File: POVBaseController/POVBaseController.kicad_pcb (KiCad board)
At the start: 2 copper layers, 24 parts, among them P1 CONN_01X02, P2 CONN_01X02, P3 CONN_01X05, U1 MPM3606, U2 CY8C4014LQI-412

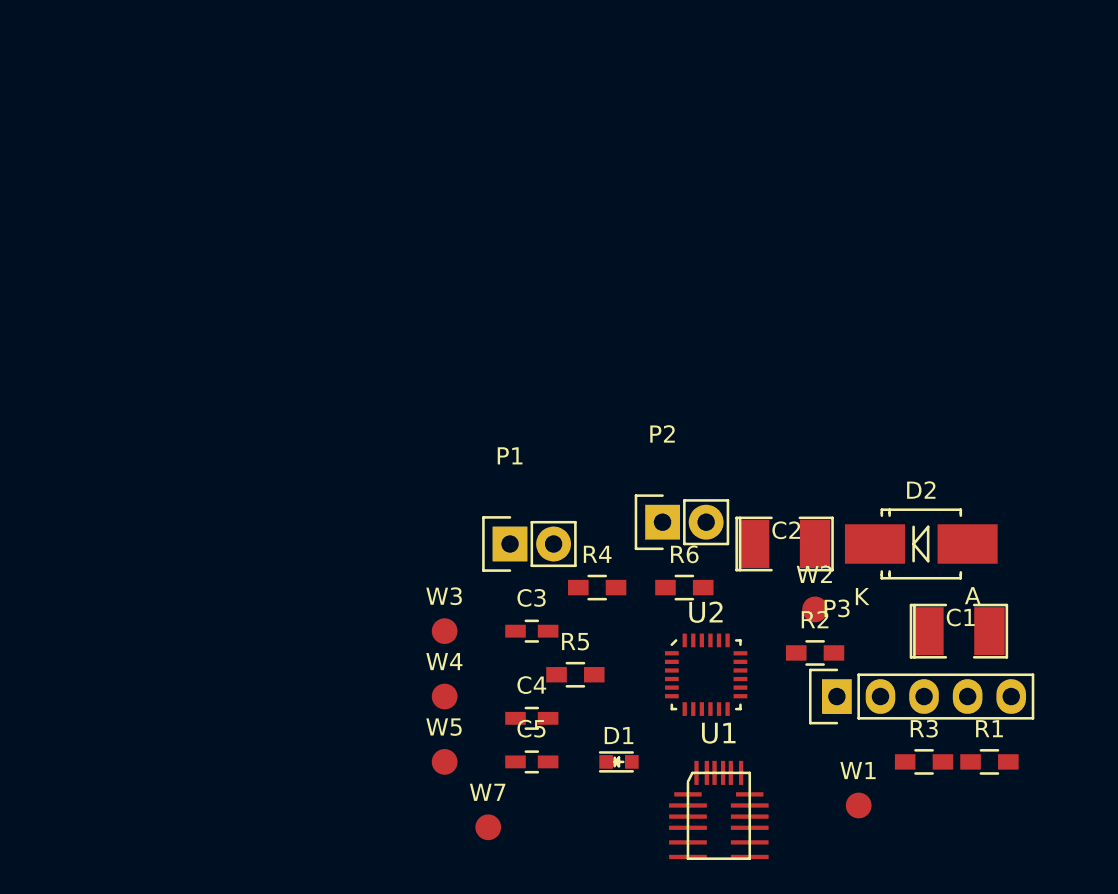
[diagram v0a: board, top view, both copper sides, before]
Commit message: Updated the design and layout with an LDO.
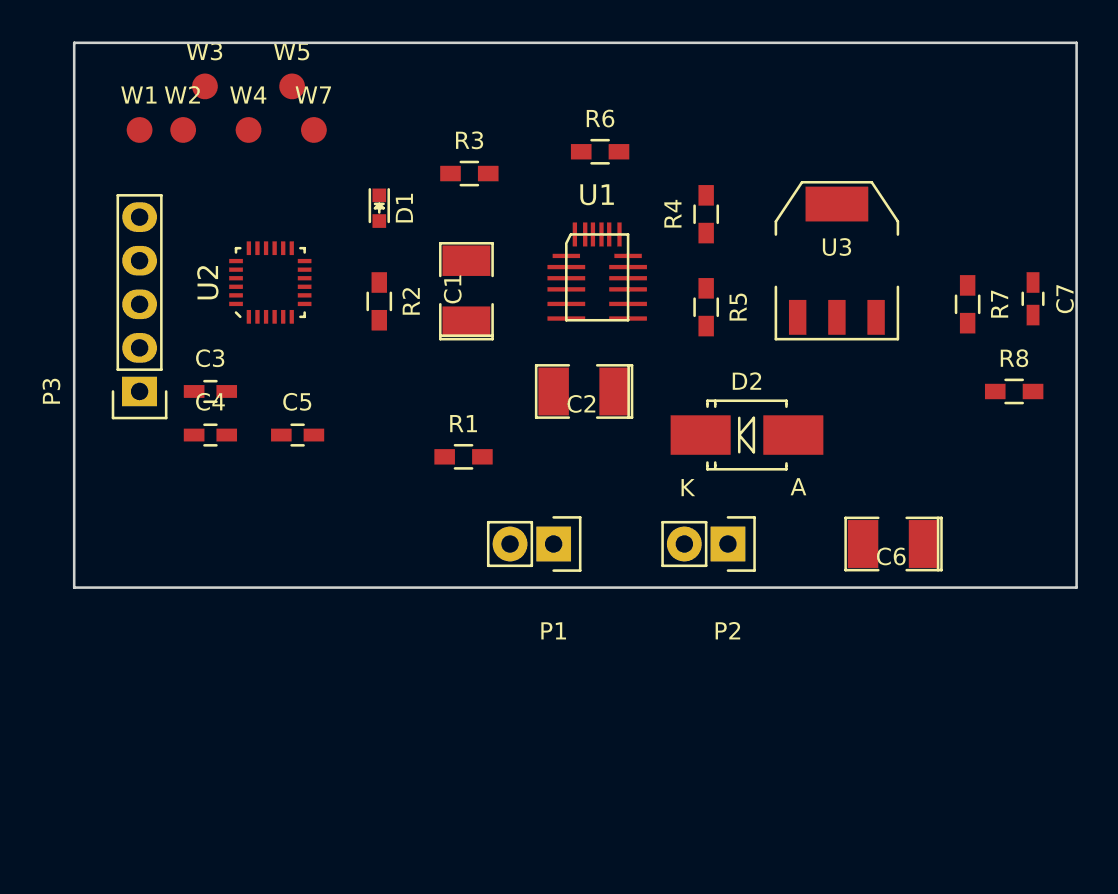
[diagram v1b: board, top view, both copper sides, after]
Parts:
- added C6: 10u, SMD_Packages:SMD-1210_Pol, F.Cu at (159.5, 97.8)
- added C7: 100u, Capacitors_SMD:C_0603_HandSoldering, F.Cu at (167.6, 83.5)
- added R7: 120, Resistors_SMD:R_0603_HandSoldering, F.Cu at (163.8, 83.8)
- added R8: 360, Resistors_SMD:R_0603_HandSoldering, F.Cu at (166.5, 88.9)
- added U3: LD1117S50CTR, TO_SOT_Packages_SMD:SOT-223, F.Cu at (156.2, 81.3)
- moved W1 57.5 mm to (115.6, 73.7)
- moved W2 46.2 mm to (118.1, 73.7)
- moved P3 44.4 mm to (115.6, 88.9), turned to 90 degrees
- moved R3 43.3 mm to (134.8, 76.2)
- moved W7 41.9 mm to (125.7, 73.7)
- moved W5 40.4 mm to (124.5, 71.1)
- moved R1 35.4 mm to (134.4, 92.7)
- moved D1 35.2 mm to (129.5, 78.2), turned to 270 degrees
- moved W4 34.9 mm to (121.9, 73.7)
- moved C1 34.9 mm to (134.6, 83.1), turned to 90 degrees
- moved W3 34.7 mm to (119.4, 71.1)
- moved U2 34.2 mm to (123.2, 82.5), turned to 90 degrees
- moved R2 32.6 mm to (129.5, 83.7), turned to 270 degrees
- moved U1 32.2 mm to (142.2, 82.5)
- moved R6 25.9 mm to (142.4, 74.9)
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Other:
- board outline added: 58.4 x 31.8 mm

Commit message: Completed the routing of the POVBaseController.
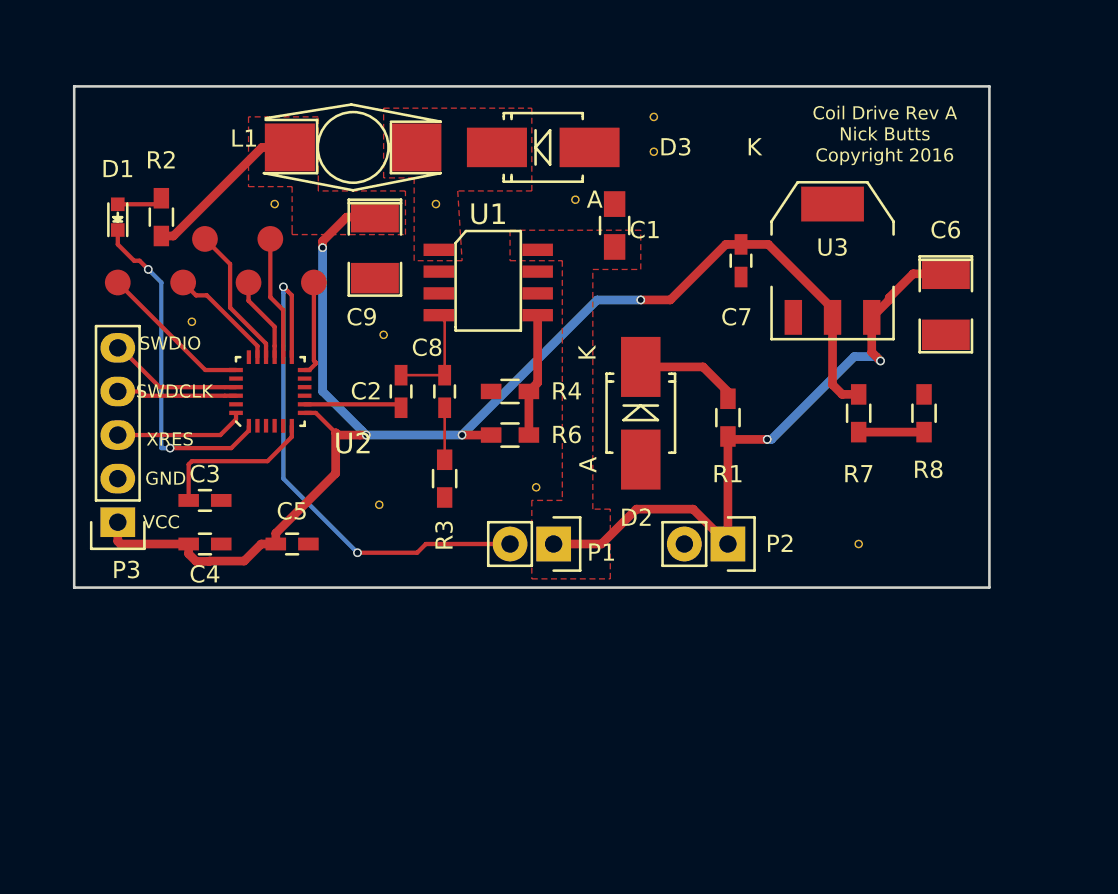
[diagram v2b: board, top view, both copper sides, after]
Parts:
- removed R5: 100K, Resistors_SMD:R_0603_HandSoldering
- added C8: 8.2n, Capacitors_SMD:C_0603_HandSoldering, F.Cu at (133.3, 88.9)
- added C9: 22u, SMD_Packages:SMD-1210_Pol, F.Cu at (129.3, 80.5)
- added D3: STPS2L40, Diodes_SMD:SMB_Handsoldering, F.Cu at (139.1, 74.7)
- added L1: 82u, myfootprint:TDK_Inductor_12.95x9.4x5.08, F.Cu at (128.0, 74.7)
- added REF**: VIA-13MILS, myfootprint:VIA-13MILS, F.Cu at (118.6, 84.8)
- added REF**: VIA-13MILS, myfootprint:VIA-13MILS, F.Cu at (157.5, 97.8)
- added REF**: VIA-13MILS, myfootprint:VIA-13MILS, F.Cu at (145.5, 72.9)
- added REF**: VIA-13MILS, myfootprint:VIA-13MILS, F.Cu at (145.5, 74.9)
- added REF**: VIA-13MILS, myfootprint:VIA-13MILS, F.Cu at (141.0, 77.7)
- added REF**: VIA-13MILS, myfootprint:VIA-13MILS, F.Cu at (132.8, 78.0)
- added REF**: VIA-13MILS, myfootprint:VIA-13MILS, F.Cu at (123.4, 78.0)
- added REF**: VIA-13MILS, myfootprint:VIA-13MILS, F.Cu at (129.8, 85.6)
- added REF**: VIA-13MILS, myfootprint:VIA-13MILS, F.Cu at (129.5, 95.5)
- added REF**: VIA-13MILS, myfootprint:VIA-13MILS, F.Cu at (138.7, 94.5)
- C1: value 10U -> 1.5u; footprint SMD_Packages:SMD-1210_Pol -> Capacitors_SMD:C_0805_HandSoldering
- C2: value 22U -> 56p; footprint SMD_Packages:SMD-1210_Pol -> Capacitors_SMD:C_0603_HandSoldering
- R3: value 100K -> 11k
- R4: value 100K -> 4.3k
- R6: value 19.1K -> 13k
- U1: value MPM3606 -> A5970AD; footprint myfootprint:QFN-20 -> myfootprint:SO-8
- moved R3 17.8 mm to (133.3, 94.0), turned to 270 degrees
- moved R6 17.3 mm to (137.2, 91.4), turned to 180 degrees
- moved C7 17.2 mm to (150.6, 81.3)
- moved R1 15.6 mm to (149.9, 90.4), turned to 90 degrees
- moved R4 15.4 mm to (137.2, 88.9), turned to 180 degrees
- moved D1 15.2 mm to (114.3, 78.7), turned to 90 degrees
- moved C6 14.3 mm to (162.6, 83.8), turned to 270 degrees
- moved R2 13.6 mm to (116.8, 78.7)
- moved C2 10.7 mm to (130.8, 88.9), turned to 270 degrees
- moved C1 9.45 mm to (143.3, 79.2)
- moved R7 8.98 mm to (157.5, 90.2)
- moved W1 8.98 mm to (114.3, 82.5)
- moved W5 8.98 mm to (123.2, 80.0)
- moved W2 8.89 mm to (118.1, 82.5)
- moved W3 8.89 mm to (119.4, 80.0)
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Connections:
- C2 pad 1: VCC -> Net-(C2-Pad1)
- R3 pad 1: +12V -> Net-(C8-Pad2)
- R3 pad 2: Net-(R3-Pad2) -> GND
- R4 pad 1: VCC -> Net-(R4-Pad1)
- R4 pad 2: Net-(R4-Pad2) -> GND
- R6 pad 1: Net-(R5-Pad2) -> Net-(R4-Pad1)
- R6 pad 2: GND -> VCC
- U1 pad 1: Net-(R5-Pad2) -> Net-(D3-Pad1)
- U1 pad 2: Net-(U1-Pad2) -> (no net)
- U1 pad 4: Net-(U1-Pad4) -> Net-(C2-Pad1)
- U1 pad 5: Net-(U1-Pad5) -> Net-(R4-Pad1)
- U1 pad 6: Net-(U1-Pad6) -> (no net)
- U1 pad 7: VCC -> GND
- U1 pad 8: VCC -> +12V
- U2 pad 10: Net-(U2-Pad10) -> (no net)
- U2 pad 11: Net-(U2-Pad11) -> (no net)
- U2 pad 2: Net-(U2-Pad2) -> (no net)
- U2 pad 20: Net-(U2-Pad20) -> (no net)
- U2 pad 23: Net-(U2-Pad23) -> (no net)
- U2 pad 3: Net-(U2-Pad3) -> (no net)
- U2 pad 4: Net-(U2-Pad4) -> (no net)
- U2 pad 5: Net-(U2-Pad5) -> (no net)
- U2 pad 9: Net-(U2-Pad9) -> (no net)
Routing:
- net VCC: track 0.00 -> 90.8 mm, vias 0 -> 4
- net +12V: track 0.00 -> 37.6 mm, vias 0 -> 2
- net /COIL_DR: track 0.00 -> 30.7 mm, vias 0 -> 2
- net /LED: track 0.00 -> 19.8 mm, vias 0 -> 2
- net GND: track 0.00 -> 9.55 mm
- net Net-(C3-Pad1): track 0.00 -> 9.42 mm
- net Net-(U2-Pad19): track 0.00 -> 9.00 mm
- net Net-(U2-Pad16): track 0.00 -> 8.36 mm
- net /SWDIO: track 0.00 -> 7.84 mm
- net /XRES: track 0.00 -> 7.64 mm
- net Net-(U2-Pad14): track 0.00 -> 7.20 mm
- net Net-(R4-Pad1): track 0.00 -> 7.20 mm
- net /SWDCLK: track 0.00 -> 6.99 mm
- net Net-(U2-Pad17): track 0.00 -> 6.51 mm
- net Net-(C2-Pad1): track 0.00 -> 6.18 mm
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- added copper zone on F.Cu, net +12V
- added copper zone on B.Cu, net GND
- added copper zone on F.Cu, net GND
- added copper zone on F.Cu, net Net-(D3-Pad1)
- added copper zone on F.Cu, net VCC
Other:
- board size 58.4 x 31.8 mm -> 53.3 x 29.2 mm
- rule trace_min: 0.2 -> 0.1524
- rule via_min_size: 0.4 -> 0.3302
- board text added: "Coil Drive Rev A Nick Butts Copyright 2016"
- board text added: "GND"
- board text added: "SWDCLK"
- board text added: "SWDIO"
- board text added: "VCC"
- board text added: "XRES"

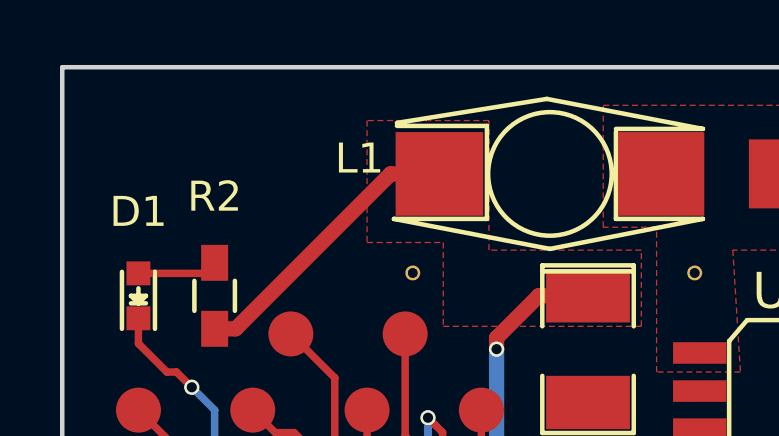
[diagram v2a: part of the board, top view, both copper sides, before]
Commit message: Ordering the POVBaseController
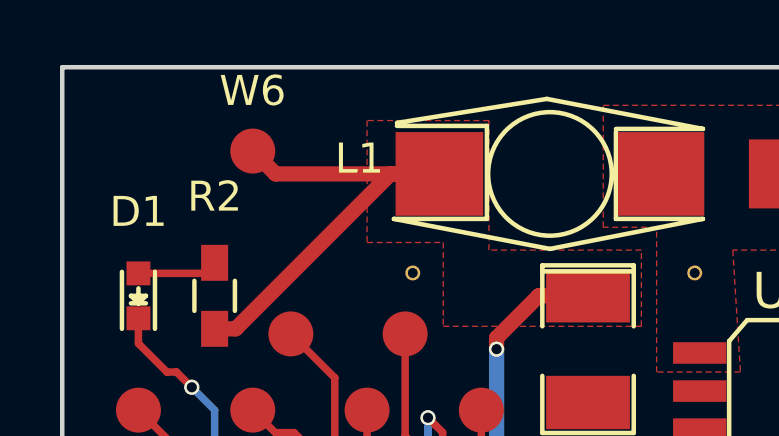
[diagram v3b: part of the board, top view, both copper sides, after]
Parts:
- added W6: TEST_1P, Measurement_Points:Measurement_Point_Round-SMD-Pad_Small, F.Cu at (118.1, 73.9)
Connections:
- U1 pad 2: (no net) -> Net-(U1-Pad2)
- U1 pad 6: (no net) -> Net-(U1-Pad6)
- U2 pad 10: (no net) -> Net-(U2-Pad10)
- U2 pad 11: (no net) -> Net-(U2-Pad11)
- U2 pad 2: (no net) -> Net-(U2-Pad2)
- U2 pad 20: (no net) -> Net-(U2-Pad20)
- U2 pad 23: (no net) -> Net-(U2-Pad23)
- U2 pad 3: (no net) -> Net-(U2-Pad3)
- U2 pad 4: (no net) -> Net-(U2-Pad4)
- U2 pad 5: (no net) -> Net-(U2-Pad5)
- U2 pad 9: (no net) -> Net-(U2-Pad9)
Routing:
- net VCC: track 90.8 -> 97.3 mm
